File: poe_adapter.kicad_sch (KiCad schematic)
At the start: 16 parts

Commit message: buck converter init
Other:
- added sheet LM5116 DCDC Converter (lm5116_synchronous_buck.kicad_sch)
- note added: "LM5116 Synchronous Buck Converter"
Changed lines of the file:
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@@
+    (stroke (width 0) (type default) (color 0 0 0 0))
+  )
+  (polyline (pts (xy 163.195 76.2) (xy 163.83 172.72))
     (stroke (width 0) (type default) (color 0 0 0 0))
   )
@@
   )
   (text "ESD Protection\n" (at 44.45 66.675 90)
+    (effects (font (size 1.27 1.27)) (justify left bottom))
+  )
+  (text "LM5116 Synchronous Buck Converter" (at 163.83 78.74 0)
     (effects (font (size 1.27 1.27)) (justify left bottom))
   )
@@
     (pin "1")
   )
-  (sheet (at 90.805 85.725) (size 27.94 19.05) (fields_autoplaced)
+  (sheet (at 176.53 104.14) (size 34.29 21.59) (fields_autoplaced)
     (stroke (width 0.1524) (type solid) (color 0 0 0 0))
     (fill (color 0 0 0 0.0000))
-    (property "Sheet name" "TPS2372 Sub System" (id 0) (at 90.805 85.0134 0)
+    (property "Sheet name" "LM5116 DCDC Converter" (id 0) (at 176.53 103.4284 0)
       (effects (font (size 1.27 1.27)) (justify left bottom))
     )
-    (property "Sheet file" "TPS2372.kicad_sch" (id 1) (at 90.805 105.3596 0)
+    (property "Sheet file" "lm5116_synchronous_buck.kicad_sch" (id 1) (at 176.53 126.3146 0)
       (effects (font (size 1.27 1.27)) (justify left top))
     )
-    (pin "TCTB" input (at 90.805 93.345 180)
-      (effects (font (size 1.27 1.27)) (justify left))
-    )
-    (pin "TCTD" input (at 90.805 99.695 180)
-      (effects (font (size 1.27 1.27)) (justify left))
-    )
-    (pin "TCTC" input (at 90.805 96.52 180)
-      (effects (font (size 1.27 1.27)) (justify left))
-    )
-    (pin "TCTA" input (at 90.805 90.17 180)
-      (effects (font (size 1.27 1.27)) (justify left))
-    )
-    (pin "PoE_48VOUT" output (at 118.745 90.17 0)
+  )
+  (sheet (at 106.045 106.045) (size 27.94 19.05) (fields_autoplaced)
+    (stroke (width 0.1524) (type solid) (color 0 0 0 0))
+    (fill (color 0 0 0 0.0000))
+    (property "Sheet name" "TPS2372 Sub System" (id 0) (at 106.045 105.3334 0)
+      (effects (font (size 1.27 1.27)) (justify left bottom))
+    )
+    (property "Sheet file" "TPS2372.kicad_sch" (id 1) (at 106.045 125.6796 0)
+      (effects (font (size 1.27 1.27)) (justify left top))
+    )
+    (pin "TCTB" input (at 106.045 113.665 180)
+      (effects (font (size 1.27 1.27)) (justify left))
+    )
+    (pin "TCTD" input (at 106.045 120.015 180)
+      (effects (font (size 1.27 1.27)) (justify left))
+    )
+    (pin "TCTC" input (at 106.045 116.84 180)
+      (effects (font (size 1.27 1.27)) (justify left))
+    )
+    (pin "TCTA" input (at 106.045 110.49 180)
+      (effects (font (size 1.27 1.27)) (justify left))
+    )
+    (pin "PoE_48VOUT" output (at 133.985 110.49 0)
       (effects (font (size 1.27 1.27)) (justify right))
     )
-    (pin "PoE_RTN" output (at 118.745 93.345 0)
+    (pin "PoE_RTN" output (at 133.985 113.665 0)
       (effects (font (size 1.27 1.27)) (justify right))
     )
@@
     (path "/9d43f031-4287-4645-997e-8ec53611a4dd" (page "2"))
     (path "/51efc304-0253-4cf9-b8a4-37a603089f63" (page "3"))
+    (path "/2ca3a0f2-1db2-49ca-b941-3735f746c2ef" (page "4"))
   )
   (symbol_instances
@@
       (reference "TR?") (unit 1) (value "TG111-MSC13LF") (footprint "Transformer_SMD:Transformer_Ethernet_HALO_TG111-MSC13")
     )
+    (path "/2ca3a0f2-1db2-49ca-b941-3735f746c2ef/0d05a586-02a5-4a43-a481-a713afbab191"
+      (reference "U?") (unit 1) (value "LM5116") (footprint "Package_SO:HTSSOP-20-1EP_4.4x6.5mm_P0.65mm_EP2.85x4mm")
+    )
     (path "/9d43f031-4287-4645-997e-8ec53611a4dd/0f631ae3-94bb-4ff1-a424-728f55d1bf23"

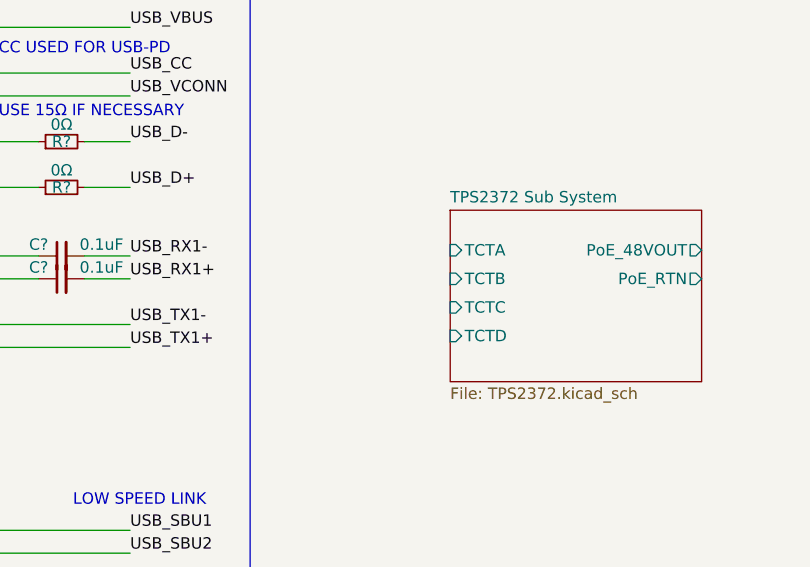
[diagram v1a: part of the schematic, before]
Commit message: TPS2372 Modified, test jumpers removed
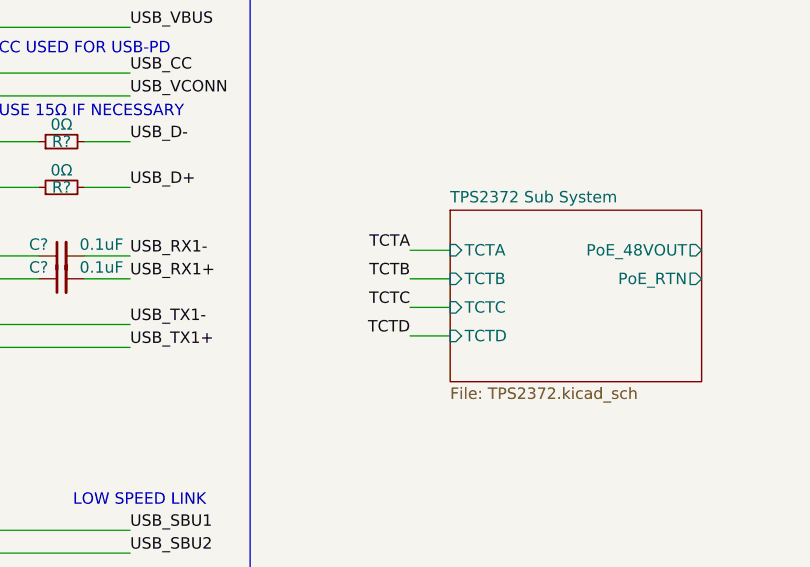
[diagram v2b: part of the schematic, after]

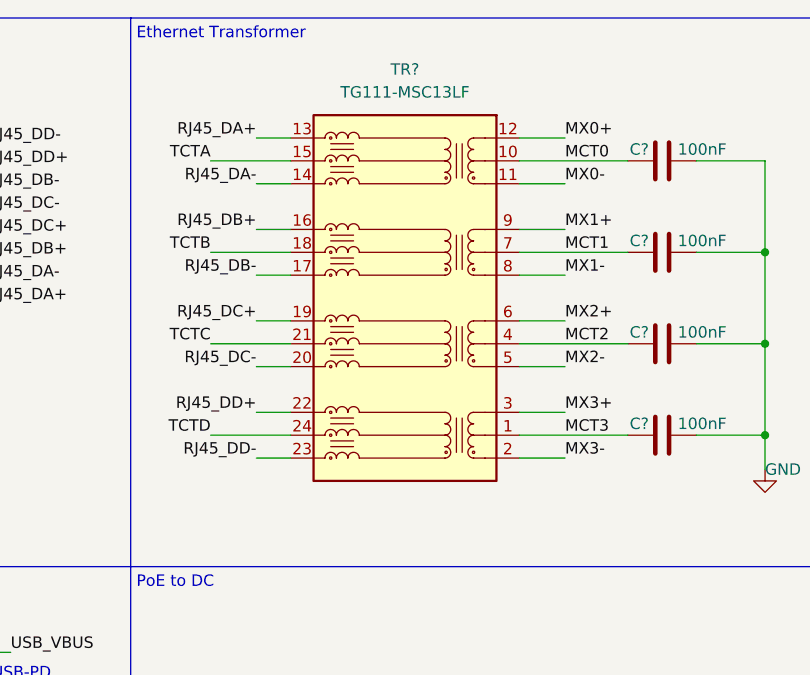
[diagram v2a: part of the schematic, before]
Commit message: PoE TR change to 7490220122; updated pwr net
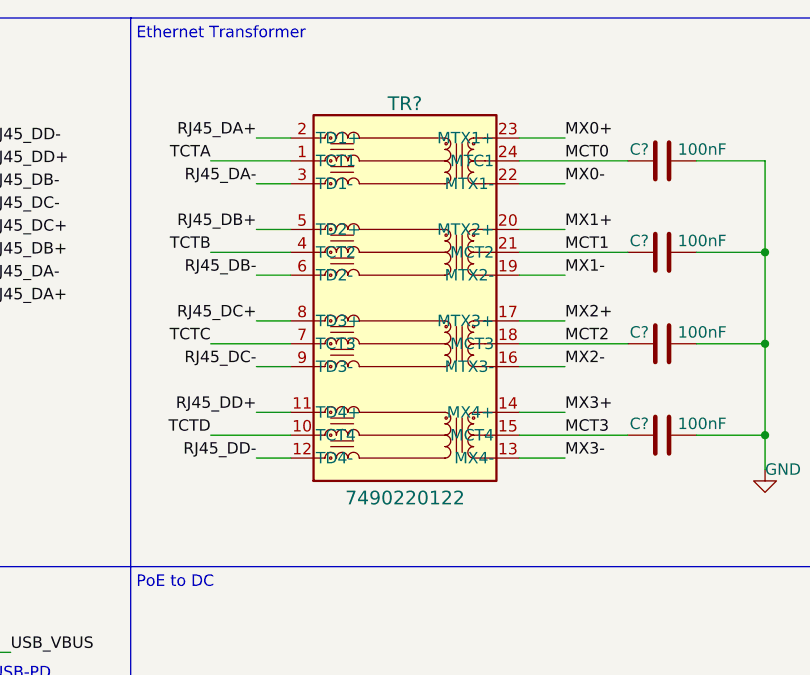
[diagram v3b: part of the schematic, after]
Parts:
- removed TR?: TG111-MSC13LF, Transformer_SMD:Transformer_Ethernet_HALO_TG111-MSC13, symbol Transformer:TG111-MSC13LF
- added TR?: 7490220122, 7490220122_WRE, symbol 7490220122:7490220122
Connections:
- net MCT0: now also TR?.24 (MTC1)
- net MCT1: now also TR?.21 (MCT2)
- net MCT2: now also TR?.18 (MCT3)
- net MCT3: now also TR?.15 (MCT4)
- net MX0+: now also TR?.23 (MTX1+)
- net MX0-: now also TR?.22 (MTX1-)
- net MX1+: now also TR?.20 (MTX2+)
- net MX1-: now also TR?.19 (MTX2-)
- net MX2+: now also TR?.17 (MTX3+)
- net MX2-: now also TR?.16 (MTX3-)
- net MX3+: now also TR?.14 (MX4+)
- net MX3-: now also TR?.13 (MX4-)
- net RJ45_DA+: now also TR?.2 (TD1+)
- net RJ45_DA-: now also TR?.3 (TD1-)
- net RJ45_DB+: now also TR?.5 (TD2+)
- net RJ45_DB-: now also TR?.6 (TD2-)
- net RJ45_DC+: now also TR?.8 (TD3+)
- net RJ45_DC-: now also TR?.9 (TD3-)
- net RJ45_DD+: now also TR?.11 (TD4+)
- net RJ45_DD-: now also TR?.12 (TD4-)
- net TCTA: now also TR?.1 (TCT1)
- net TCTB: now also TR?.4 (TCT2)
- net TCTC: now also TR?.7 (TCT3)
- net TCTD: now also TR?.10 (TCT4)
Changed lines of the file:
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@@
     (pin "2")
-  )
-  (symbol (lib_id "Transformer:TG111-MSC13LF") (at 114.3 46.355 0) (unit 1)
-    (in_bom yes) (on_board yes) (fields_autoplaced)
-    (property "Reference" "TR?" (id 0) (at 114.3 20.955 0))
-    (property "Value" "TG111-MSC13LF" (id 1) (at 114.3 23.495 0))
-    (property "Footprint" "Transformer_SMD:Transformer_Ethernet_HALO_TG111-MSC13" (id 2) (at 114.3 67.945 0)
-      (effects (font (size 1.27 1.27)) hide)
-    )
-    (property "Datasheet" "https://www.haloelectronics.com/pdf/discrete-genesus.pdf" (id 3) (at 116.84 22.225 0)
-      (effects (font (size 1.27 1.27)) hide)
-    )
-    (pin "1")
-    (pin "10")
-    (pin "11")
-    (pin "12")
-    (pin "13")
-    (pin "14")
-    (pin "15")
-    (pin "16")
-    (pin "17")
-    (pin "18")
-    (pin "19")
-    (pin "2")
-    (pin "20")
-    (pin "21")
-    (pin "22")
-    (pin "23")
-    (pin "24")
-    (pin "3")
-    (pin "4")
-    (pin "5")
-    (pin "6")
-    (pin "7")
-    (pin "8")
-    (pin "9")
   )
   (symbol (lib_id "Device:C_Small") (at 62.865 113.665 90) (unit 1)
@@
     (pin "2")
   )
+  (symbol (lib_id "7490220122:7490220122") (at 93.345 31.115 0) (unit 1)
+    (in_bom yes) (on_board yes)
+    (property "Reference" "TR?" (id 0) (at 114.3 24.765 0)
+      (effects (font (size 1.524 1.524)))
+    )
+    (property "Value" "7490220122" (id 1) (at 114.3 68.58 0)
+      (effects (font (size 1.524 1.524)))
+    )
+    (property "Footprint" "7490220122_WRE" (id 2) (at 113.665 25.019 0)
+      (effects (font (size 1.524 1.524)) hide)
+    )
+    (property "Datasheet" "https://www.we-online.com/catalog/datasheet/7490220122.pdf" (id 3) (at 114.3 24.13 0)
+      (effects (font (size 1.524 1.524)) hide)
+    )
+    (pin "1")
+    (pin "10")
+    (pin "11")
+    (pin "12")
+    (pin "13")
+    (pin "14")
+    (pin "15")
+    (pin "16")
+    (pin "17")
+    (pin "18")
+    (pin "19")
+    (pin "2")
+    (pin "20")
+    (pin "21")
+    (pin "22")
+    (pin "23")
+    (pin "24")
+    (pin "3")
+    (pin "4")
+    (pin "5")
+    (pin "6")
+    (pin "7")
+    (pin "8")
+    (pin "9")
+  )
   (symbol (lib_id "power:+3V3") (at 31.75 31.75 90) (unit 1)
     (in_bom yes) (on_board yes)
@@
       (reference "#PWR?") (unit 1) (value "VSS") (footprint "")
     )
-    (path "/51efc304-0253-4cf9-b8a4-37a603089f63/5731ed05-baf9-43e0-ab0c-93bbd2dd33af"
-      (reference "#PWR?") (unit 1) (value "VSSA") (footprint "")
-    )
     (path "/9d43f031-4287-4645-997e-8ec53611a4dd/5c652daf-f0c9-41a2-8e45-b57dd2248b5f"
       (reference "#PWR?") (unit 1) (value "+3V3") (footprint "")
@@
       (reference "#PWR?") (unit 1) (value "+3V3") (footprint "")
     )
-    (path "/51efc304-0253-4cf9-b8a4-37a603089f63/c1725271-b858-4155-979e-93fcef2d3882"
-      (reference "#PWR?") (unit 1) (value "+48V") (footprint "")
-    )
     (path "/9d43f031-4287-4645-997e-8ec53611a4dd/c24f0a4f-4a5f-48bc-b617-5994640a89e0"
       (reference "#PWR?") (unit 1) (value "+3V3") (footprint "")
@@
       (reference "#PWR?") (unit 1) (value "VDDA") (footprint "")
     )
-    (path "/51efc304-0253-4cf9-b8a4-37a603089f63/cf380f9b-3109-49f7-b452-2e90cc994459"
-      (reference "#PWR?") (unit 1) (value "+48V") (footprint "")
-    )
-    (path "/51efc304-0253-4cf9-b8a4-37a603089f63/d3140f95-49ba-4cbe-a8ed-40aedfb6b461"
-      (reference "#PWR?") (unit 1) (value "VSSA") (footprint "")
-    )
     (path "/9d43f031-4287-4645-997e-8ec53611a4dd/d3230b09-7f05-4628-b5c3-ab1789642c7e"
       (reference "#PWR?") (unit 1) (value "VSS") (footprint "")
@@
       (reference "TP?") (unit 1) (value "+48 Test 1") (footprint "")
     )
-    (path "/02e3c308-64f1-4854-97c3-314235fa8339"
-      (reference "TR?") (unit 1) (value "TG111-MSC13LF") (footprint "Transformer_SMD:Transformer_Ethernet_HALO_TG111-MSC13")
+    (path "/f63ab445-f771-4bf9-83e4-f80f54e503cd"
+      (reference "TR?") (unit 1) (value "7490220122") (footprint "7490220122_WRE")
     )
     (path "/2ca3a0f2-1db2-49ca-b941-3735f746c2ef/0d05a586-02a5-4a43-a481-a713afbab191"

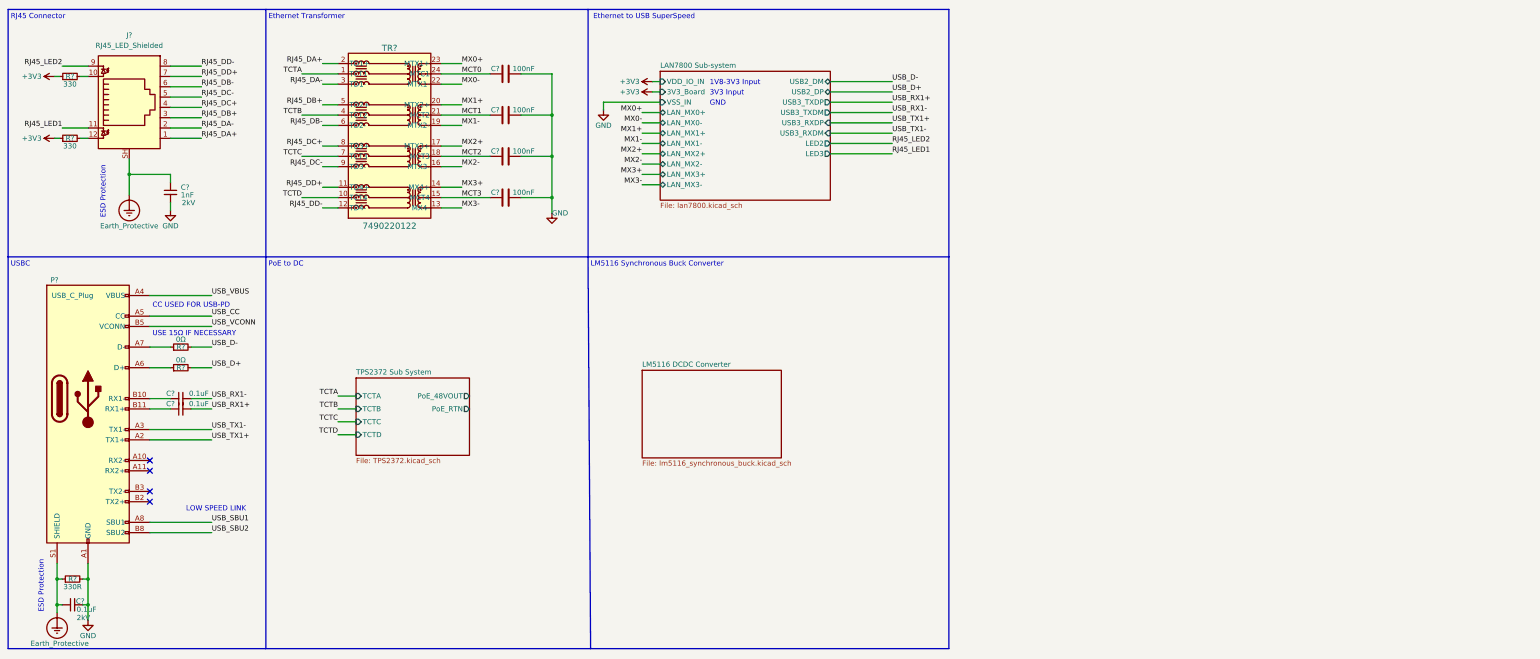
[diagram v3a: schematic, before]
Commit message: LM2575 added, provide 3V3
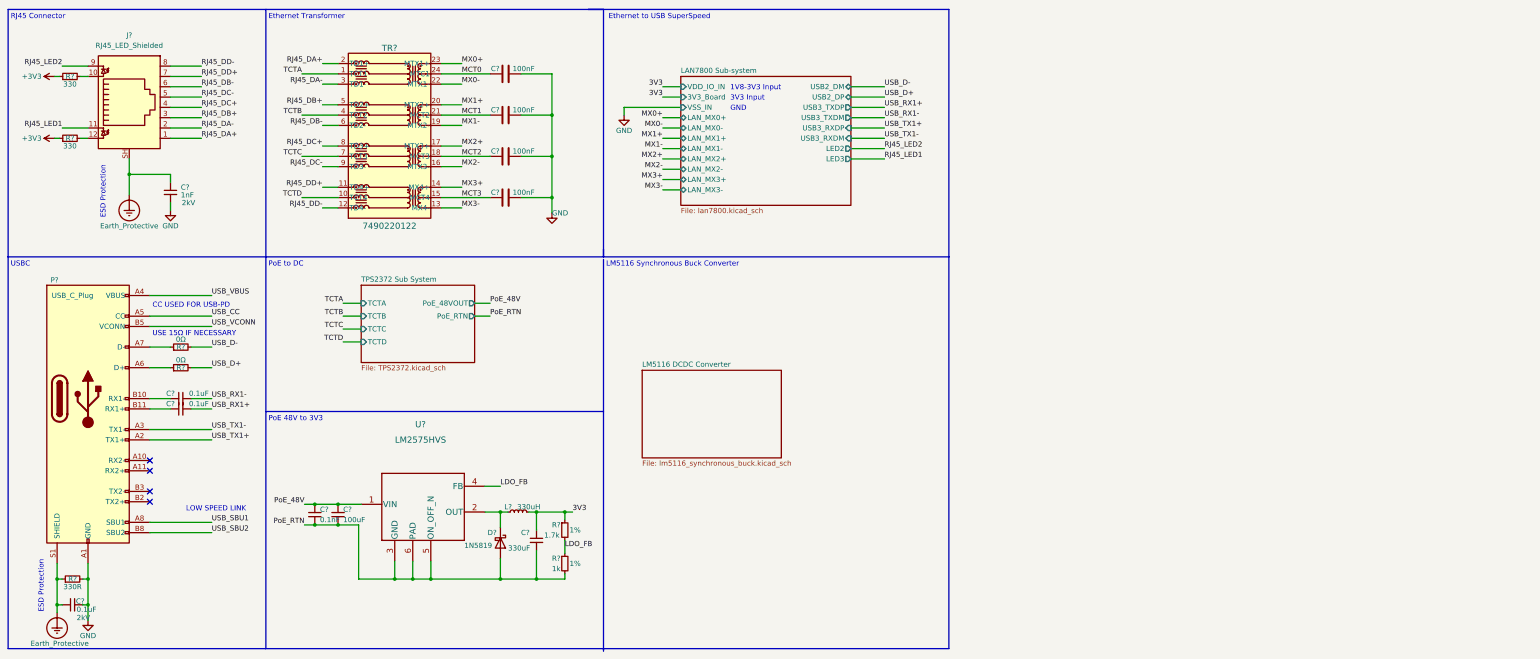
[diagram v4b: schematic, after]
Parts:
- added C?: 330uF, symbol Device:C_Small
- added C?: 100uF, symbol Device:C_Small
- added C?: 0.1nF, symbol Device:C_Small
- added D?: 1N5819, Diode_THT:D_DO-41_SOD81_P10.16mm_Horizontal, symbol Diode:1N5819
- added L?: 330uH, symbol Device:L_Small
- added R?: 1k, symbol Device:R_Small
- added R?: 1.7k, symbol Device:R_Small
- added U?: LM2575HVS, KTT0005B, symbol LM2575HV:LM2575HVS
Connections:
- new net: D?.1 (K), L?.1, U?.2 (OUT)
- new net 3V3: C?.1, L?.2, R?.1
- new net LDO_FB: R?.1, R?.2, U?.4 (FB)
- new net PoE_48V: C?.1, C?.1, U?.1 (VIN)
- new net PoE_RTN: C?.2, C?.2, C?.2, D?.2 (A), R?.2, U?.3 (GND), U?.5 (ON_OFF_N), U?.6 (PAD)
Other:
- note added: "PoE 48V to 3V3"

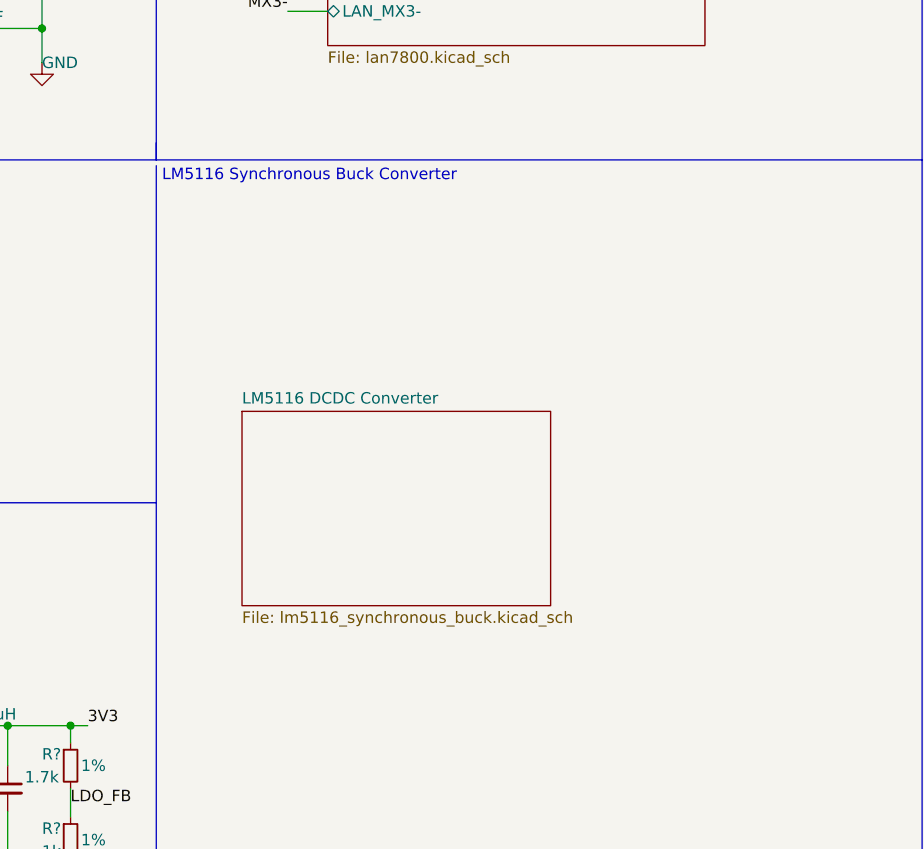
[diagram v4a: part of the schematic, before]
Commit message: * put lm5116 symbol to its own folder
* added stusb4700 symbol
* finished DCDC converter schema
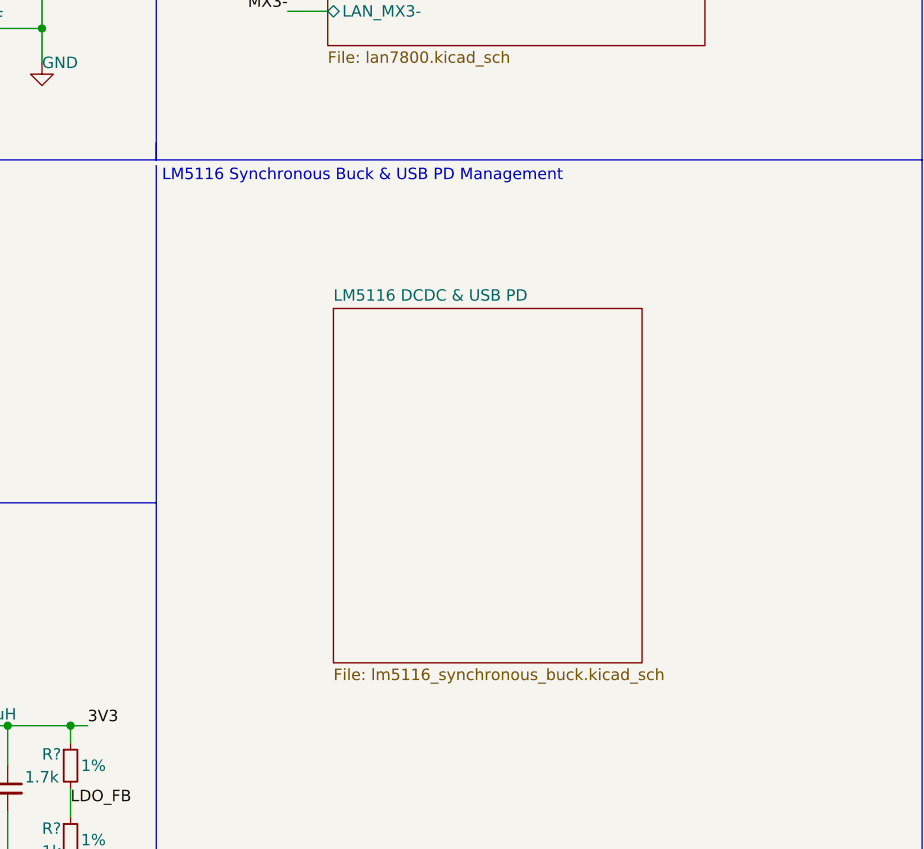
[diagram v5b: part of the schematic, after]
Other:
- sheet LM5116 DCDC Converter renamed LM5116 DCDC & USB PD
- note added: "LM5116 Synchronous Buck & USB PD Management"
- note removed: "LM5116 Synchronous Buck Converter"
- company: Zihao Pu -> Zihao Pu,  Yuqi Fu
